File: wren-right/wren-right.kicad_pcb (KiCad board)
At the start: 2 copper layers, 151.7 x 117 mm, 61 parts, among them J1 TRRS_Jack, SW0 Reset, U1 Elite C

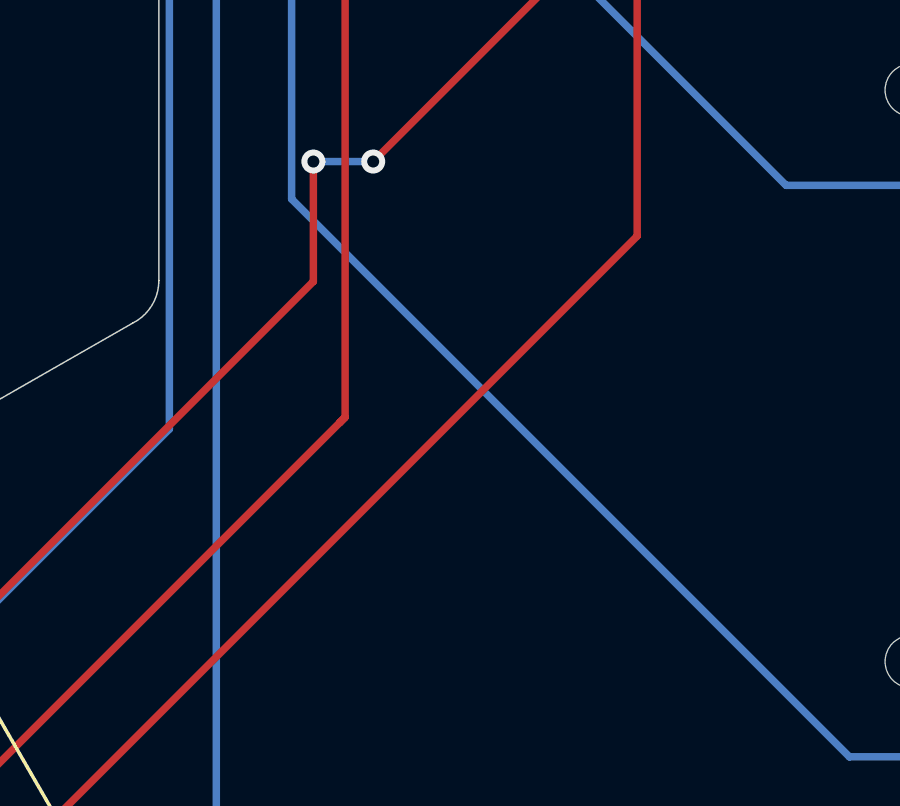
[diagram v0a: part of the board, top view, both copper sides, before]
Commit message: Add Encoders to PCB
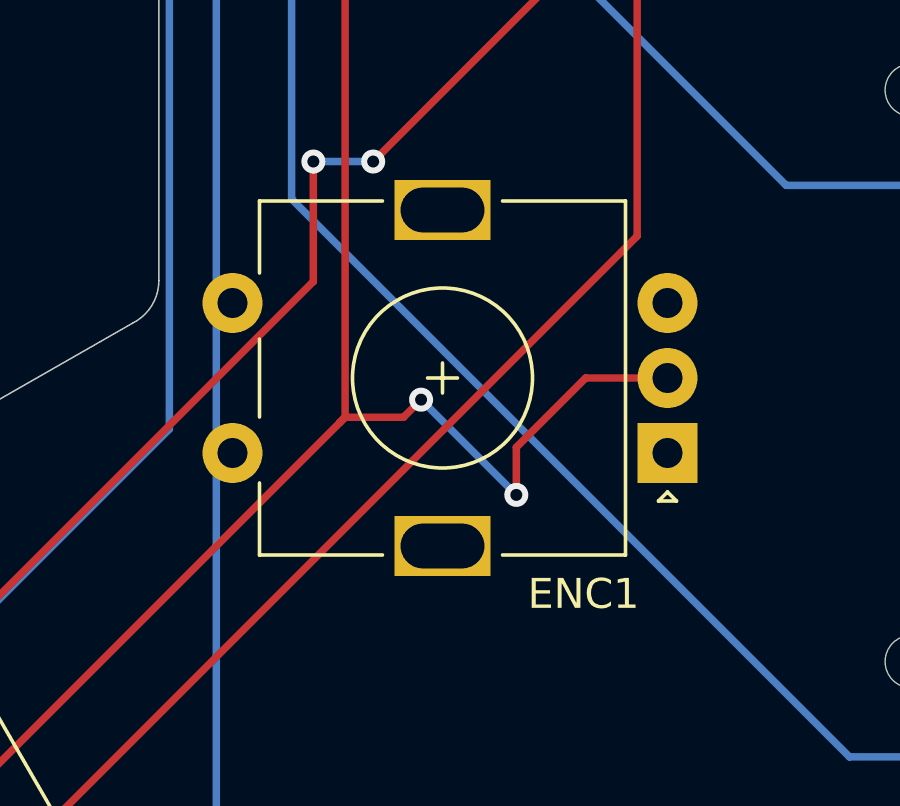
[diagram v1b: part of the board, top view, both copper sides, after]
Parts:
- added ENC1: Rotary_Encoder_Switch, Rotary_Encoder:RotaryEncoder_Alps_EC11E-Switch_Vertical_H20mm, F.Cu at (105.0, 106.6)
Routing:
- net GND: track 92.9 -> 107.8 mm, vias 0 -> 2

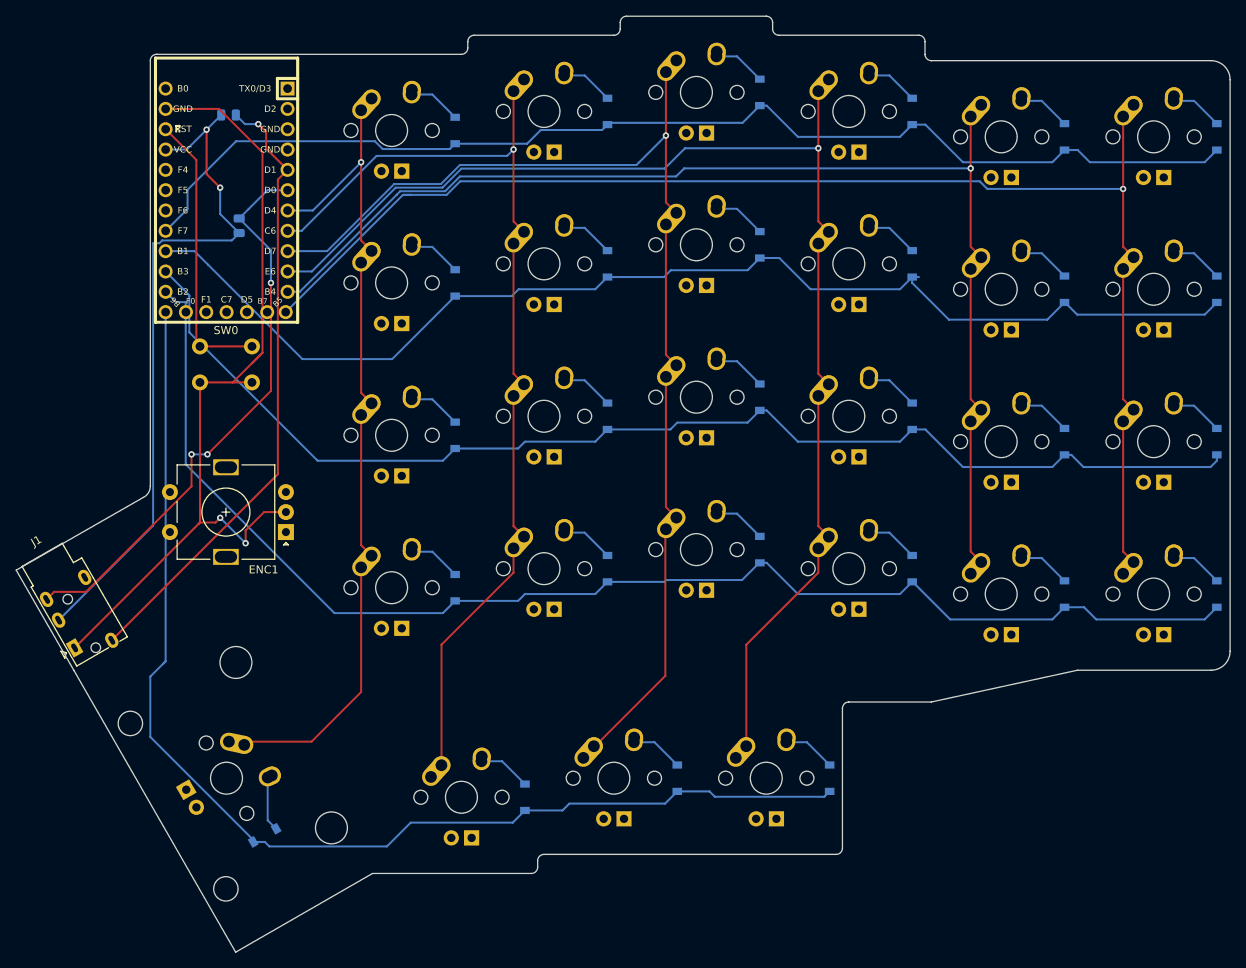
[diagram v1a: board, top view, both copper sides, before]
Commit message: Component Updates
Switch to through-hole diodes and resistors, reroute traces, etc.
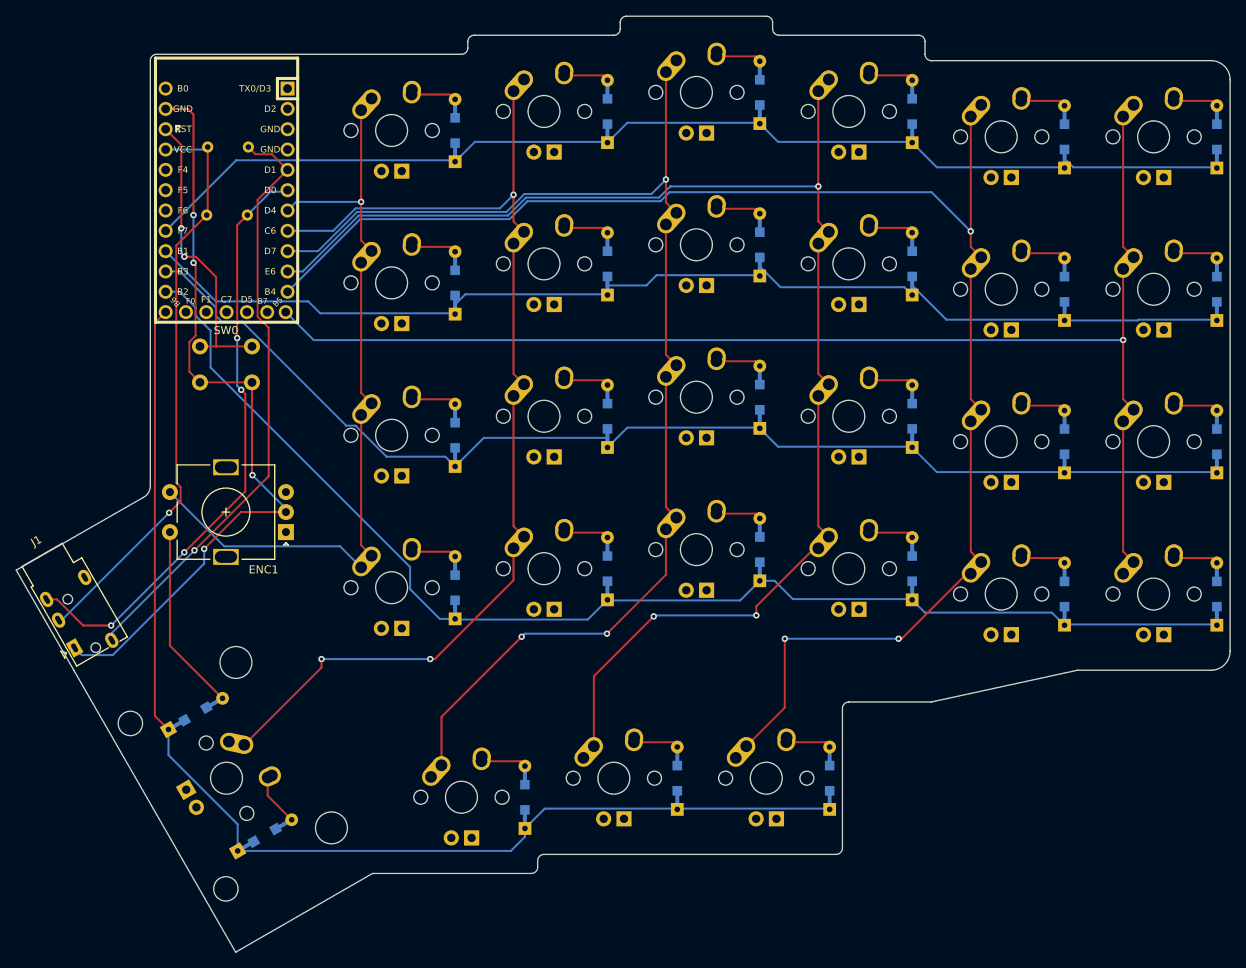
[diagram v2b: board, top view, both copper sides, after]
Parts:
- added D41: D_Small, footprints:D_SOD123_axial, B.Cu at (93.7, 129.3)
- D1, D11, D12, D13, D14, D15, D16, D2, D21, D22, D23, D24, D25, D26, D3, D31, D32, D33, D34, D35, D36, D4, D5, D6: footprint Diode_SMD:D_SOD-123 -> footprints:D_SOD123_axial
- D42: renamed from D41; footprint Diode_SMD:D_SOD-123 -> footprints:D_SOD123_axial
- D43: renamed from D42; footprint Diode_SMD:D_SOD-123 -> footprints:D_SOD123_axial
- D44: renamed from D43; footprint Diode_SMD:D_SOD-123 -> footprints:D_SOD123_axial
- D45: renamed from D44; footprint Diode_SMD:D_SOD-123 -> footprints:D_SOD123_axial
- R1, R2: footprint Resistor_SMD:R_0805_2012Metric -> Resistor_THT:R_Axial_DIN0204_L3.6mm_D1.6mm_P5.08mm_Vertical
- moved R1 4.71 mm to (100.3, 58.4)
- moved R2 1.68 mm to (100.1, 66.9), turned to 180 degrees
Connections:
- ENC1 pad S1: (no net) -> COL0
- ENC1 pad S2: (no net) -> ENC1-OUT
- MX41 pad 1: COL0 -> COL1
- MX42 pad 1: COL1 -> COL2
- MX43 pad 1: COL2 -> COL3
- MX44 pad 1: COL3 -> COL4
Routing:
- net COL4: track 146.2 -> 189.0 mm, vias 1 -> 3
- net ENC1-OUT: track 0.00 -> 23.5 mm
- net VCC: track 86.8 -> 72.9 mm, vias 2 -> 1
- net COL3: track 155.6 -> 169.2 mm, vias 1 -> 3
- net COL1: track 117.7 -> 131.3 mm, vias 1 -> 3
- net COL2: track 140.5 -> 152.5 mm, vias 1 -> 3
- net ROW3: track 168.6 -> 157.7 mm
- net GND: track 107.8 -> 98.0 mm, vias 2 -> 4
- net ROW1: track 150.1 -> 140.3 mm
- net COL0: track 100.8 -> 91.8 mm
- net COL5: track 167.2 -> 160.5 mm
- net ROW2: track 153.1 -> 147.0 mm
- net ROW0: track 146.2 -> 140.5 mm
- net SDA: track 78.7 -> 75.1 mm
- net SCL: track 71.9 -> 74.9 mm, vias 3 -> 4
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
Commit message: Cleanup, re-add drill holes
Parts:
- added REF**: MountingHole_2.2mm_M2_Pad, MountingHole:MountingHole_2.2mm_M2_Pad, F.Cu at (203.9, 66.7)
- added REF**: MountingHole_2.2mm_M2_Pad, MountingHole:MountingHole_2.2mm_M2_Pad, F.Cu at (203.9, 104.8)
- added REF**: MountingHole_2.2mm_M2_Pad, MountingHole:MountingHole_2.2mm_M2_Pad, F.Cu at (127.7, 104.0)
- added REF**: MountingHole_2.2mm_M2_Pad, MountingHole:MountingHole_2.2mm_M2_Pad, F.Cu at (127.7, 65.9)
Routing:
- net COL0: track 91.8 -> 94.0 mm
- net COL1: track 131.3 -> 132.8 mm
- net COL4: track 189.0 -> 187.6 mm
- net COL3: track 169.2 -> 169.9 mm
